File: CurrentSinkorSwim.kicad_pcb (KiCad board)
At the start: 2 copper layers, 22 parts, among them J101 Conn_01x02, J102 Conn_01x03, J103 Conn_01x02, Q301 BUK9575, U201 LMV358, U401 LM2931D-R

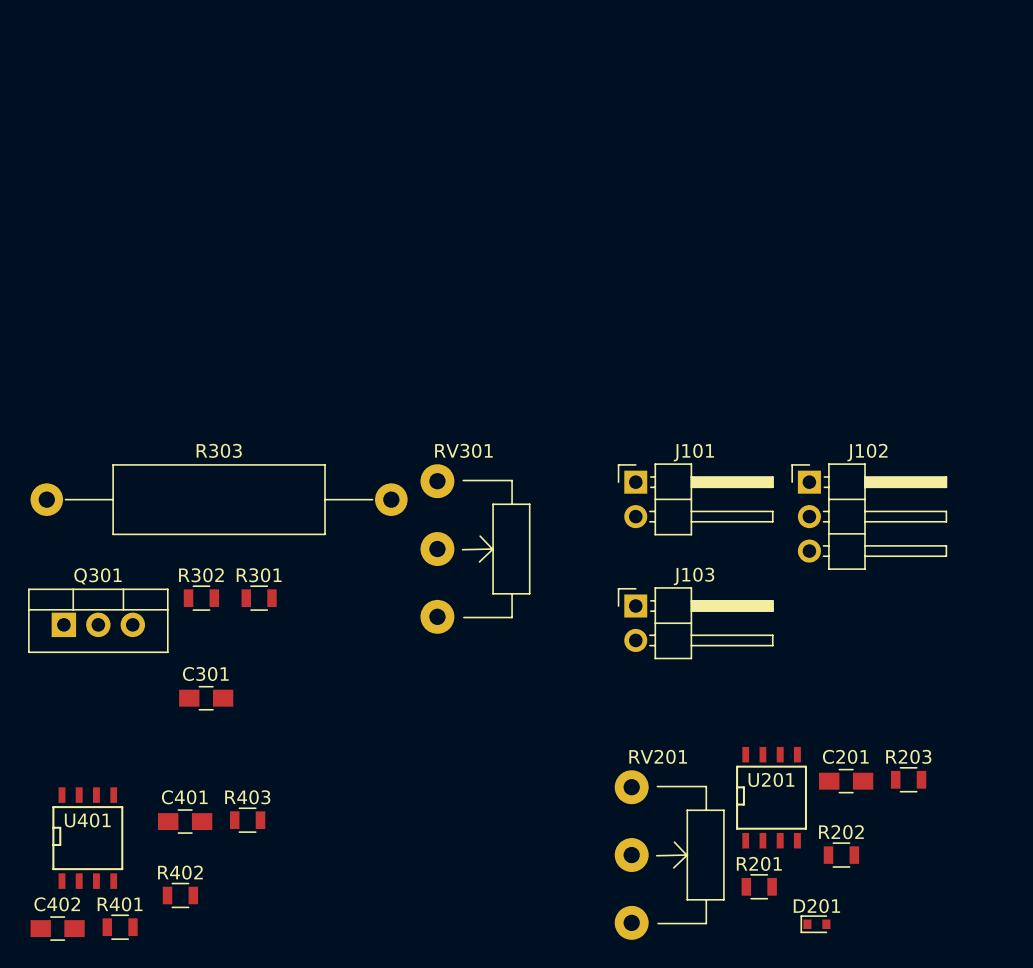
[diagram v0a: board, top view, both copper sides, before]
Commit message: Update connector footprints
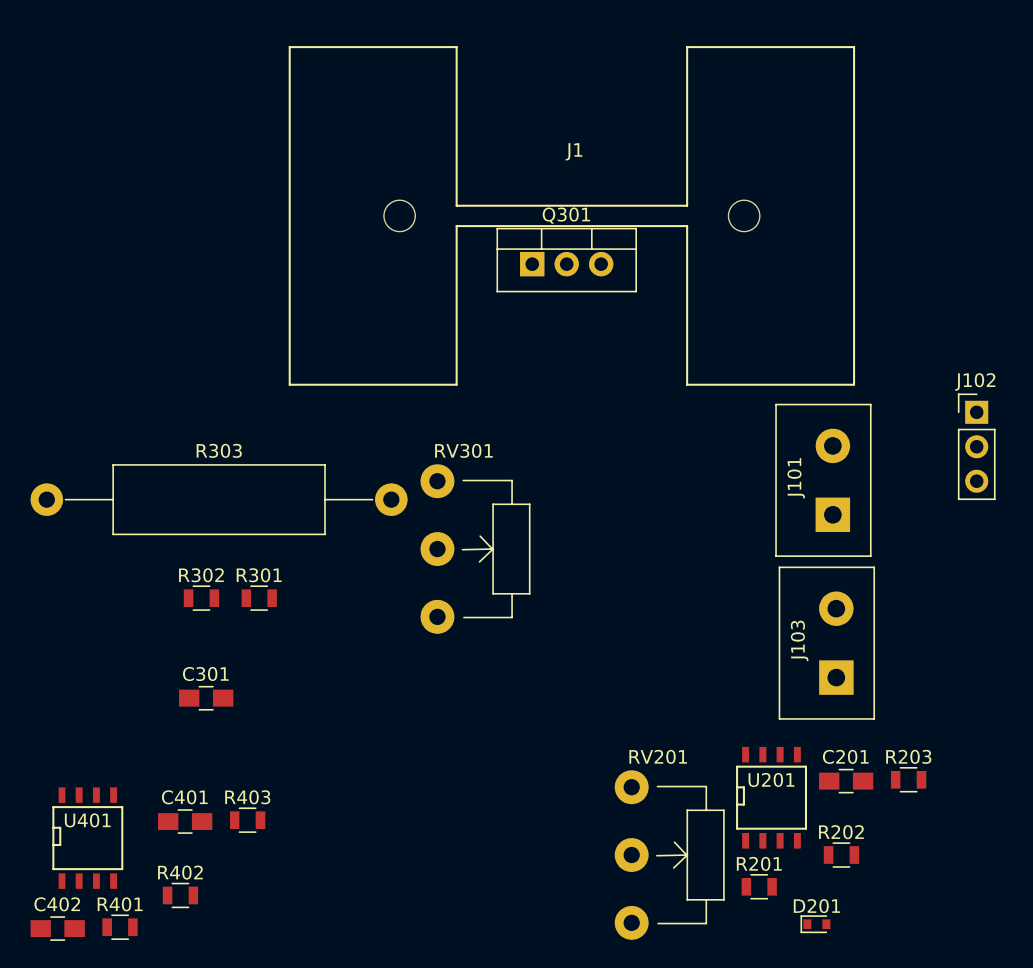
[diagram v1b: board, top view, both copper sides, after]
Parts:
- added J1: Conn_01x01, Current:FA-T220-38E, F.Cu at (196.5, 90.0)
- J101, J103: footprint Pin_Headers:Pin_Header_Angled_1x02_Pitch2.54mm -> Current:Terminal_Block_200_thou
- J102: footprint Pin_Headers:Pin_Header_Angled_1x03_Pitch2.54mm -> Pin_Headers:Pin_Header_Straight_1x03_Pitch2.54mm
- moved Q301 43.6 mm to (193.5, 93.6)
- moved J103 15.0 mm to (216.0, 121.5)
- moved J101 14.5 mm to (215.7, 109.5)
- moved J102 13.4 mm to (226.3, 104.5)
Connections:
- R201 pad 2: /Current Control/Current_Sink+ -> /Voltage Control/Current_Sink-
- R202 pad 1: Net-(R202-Pad1) -> /Current Control/Current_Sink+
- R203 pad 1: Net-(R203-Pad1) -> Net-(R202-Pad2)
- R203 pad 2: Net-(R203-Pad2) -> /Voltage Control/Current_Sink-
- U201 pad 2: /Current Control/Current_Sink+ -> Net-(R202-Pad2)

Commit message: Fixed divider resistors and found valus. Added pot footprint.
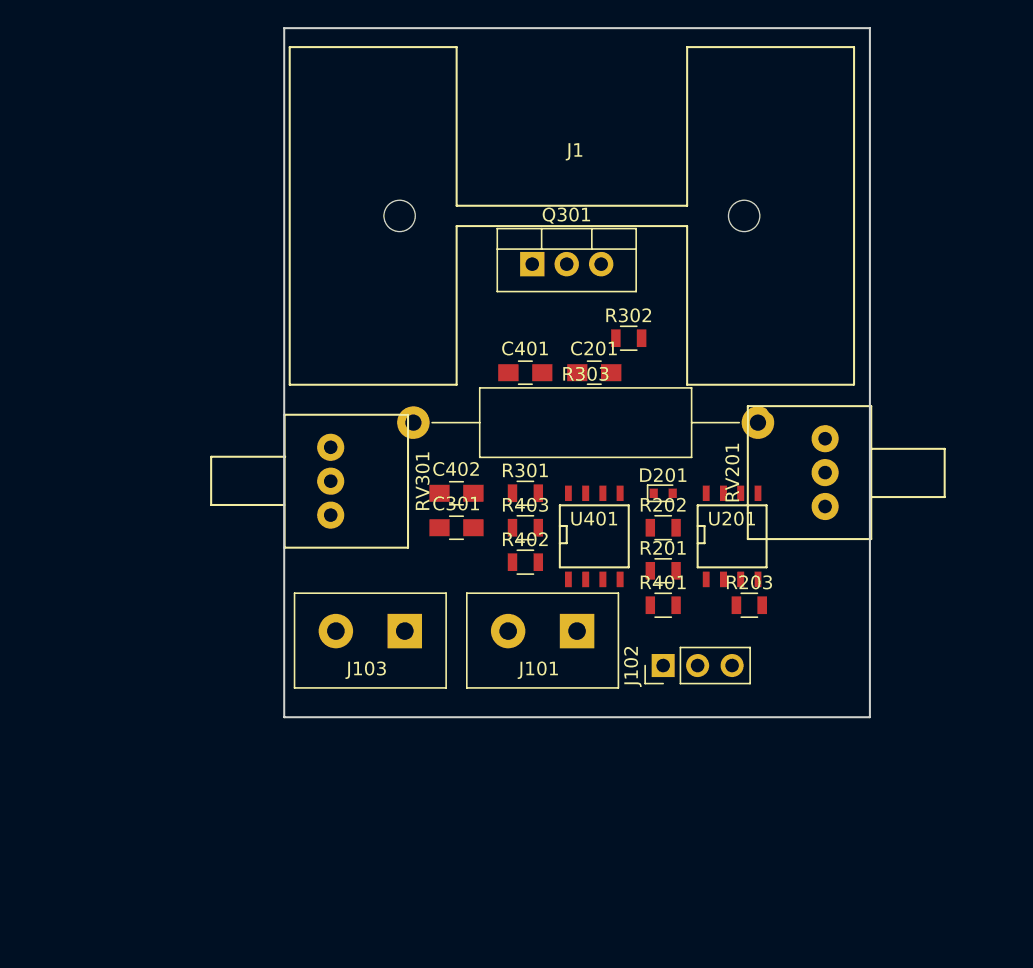
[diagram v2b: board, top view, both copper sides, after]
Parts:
- RV201, RV301: footprint Potentiometers:Potentiometer_WirePads_largePads -> Current:P090L-02F25BR10K
- moved R401 46.5 mm to (203.2, 118.7)
- moved C402 43.5 mm to (188.0, 110.5)
- moved U401 43.5 mm to (198.1, 113.7)
- moved C401 41.5 mm to (193.0, 101.6)
- moved R302 36.9 mm to (200.7, 99.1)
- moved C201 35.4 mm to (198.1, 101.6)
- moved R402 35.4 mm to (193.0, 115.6)
- moved J103 34.4 mm to (181.6, 120.7), turned to 90 degrees
- moved D201 33.7 mm to (203.2, 110.5)
- moved R403 29.7 mm to (193.0, 113.0)
- moved J102 29.7 mm to (203.2, 123.2), turned to 90 degrees
- moved R303 27.6 mm to (184.8, 105.3)
- moved R202 27.5 mm to (203.2, 113.0)
- moved RV201 27.2 mm to (215.1, 109.0), turned to 90 degrees
- moved R201 24.3 mm to (203.2, 116.2)
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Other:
- board outline added: 43.2 x 50.8 mm

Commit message: Moved components. Changed board outline. Added keepout area. Back side ground plane fill.
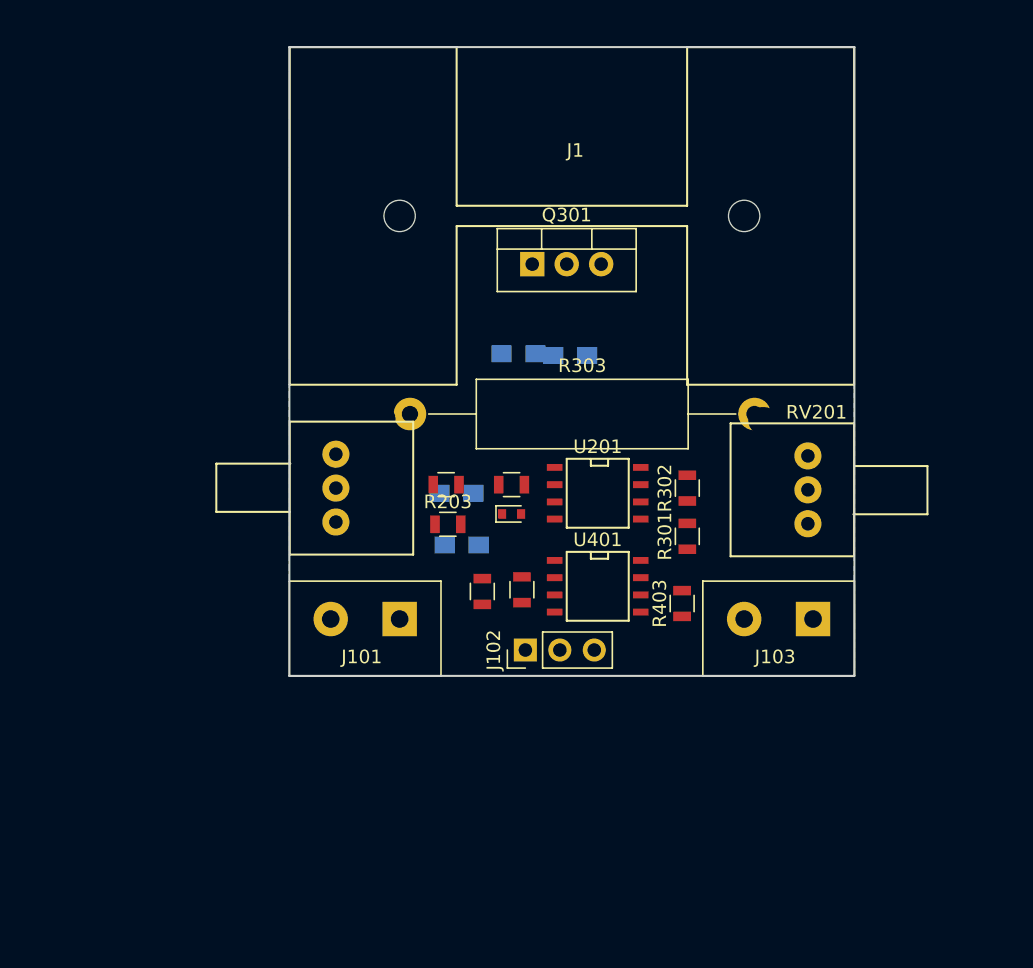
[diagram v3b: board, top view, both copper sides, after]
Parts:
- C201, C301, C401, C402: moved to B.Cu
- R201: value R -> 28.7K
- R301: value R -> 68K
- RV201, RV301: value POT -> 10K
- moved J103 30.1 mm to (211.7, 119.8)
- moved R203 23.0 mm to (187.3, 112.8)
- moved R201 17.2 mm to (187.2, 109.9)
- moved J101 13.1 mm to (181.2, 119.8)
- moved R403 12.8 mm to (204.6, 118.6), turned to 90 degrees
- moved R301 12.4 mm to (205.0, 113.7), turned to 90 degrees
- moved R302 11.9 mm to (205.0, 110.1), turned to 90 degrees
- moved R202 11.6 mm to (192.0, 109.9)
- moved D201 11.3 mm to (192.0, 112.0)
- moved R401 10.5 mm to (192.8, 117.6), turned to 270 degrees
- moved U201 10.4 mm to (198.4, 110.5), turned to 270 degrees
- moved J102 10.2 mm to (193.0, 122.0)
- moved R402 3.84 mm to (189.9, 117.7), turned to 90 degrees
- moved U401 3.69 mm to (198.4, 117.3), turned to 270 degrees
- moved C201 2.18 mm to (196.3, 100.3)
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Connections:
- C301 pad 1: 2.7V -> Net-(C301-Pad1)
- R201 pad 1: Net-(R201-Pad1) -> 2.7V
- R201 pad 2: /Voltage Control/Current_Sink- -> Net-(R201-Pad2)
- R301 pad 1: Net-(R301-Pad1) -> 2.7V
- R301 pad 2: GND -> Net-(R301-Pad2)
- RV201 pad 2: 2.7V -> Net-(R201-Pad2)
- RV201 pad 3: Net-(R201-Pad1) -> /Voltage Control/Current_Sink-
- RV301 pad 1: Net-(RV301-Pad1) -> Net-(R301-Pad2)
- RV301 pad 2: 2.7V -> GND
- RV301 pad 3: Net-(R301-Pad1) -> Net-(RV301-Pad3)
- U201 pad 3: Net-(R201-Pad1) -> Net-(R201-Pad2)
- U201 pad 5: Net-(R301-Pad1) -> Net-(R301-Pad2)
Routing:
- added copper zone on B.Cu, net GND
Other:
- board size 43.2 x 50.8 mm -> 41.7 x 46.4 mm
